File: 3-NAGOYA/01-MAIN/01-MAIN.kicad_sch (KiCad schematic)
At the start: 72 parts, among them J2 toLINE, J3 STS3032, J4 STS3032, J4 USB_C_Receptacle_USB2.0, J6 Front, J6 Top, Q1 2SA1015, SW1 NRST, SW2 BOOT0, U1 STM32F446RETx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

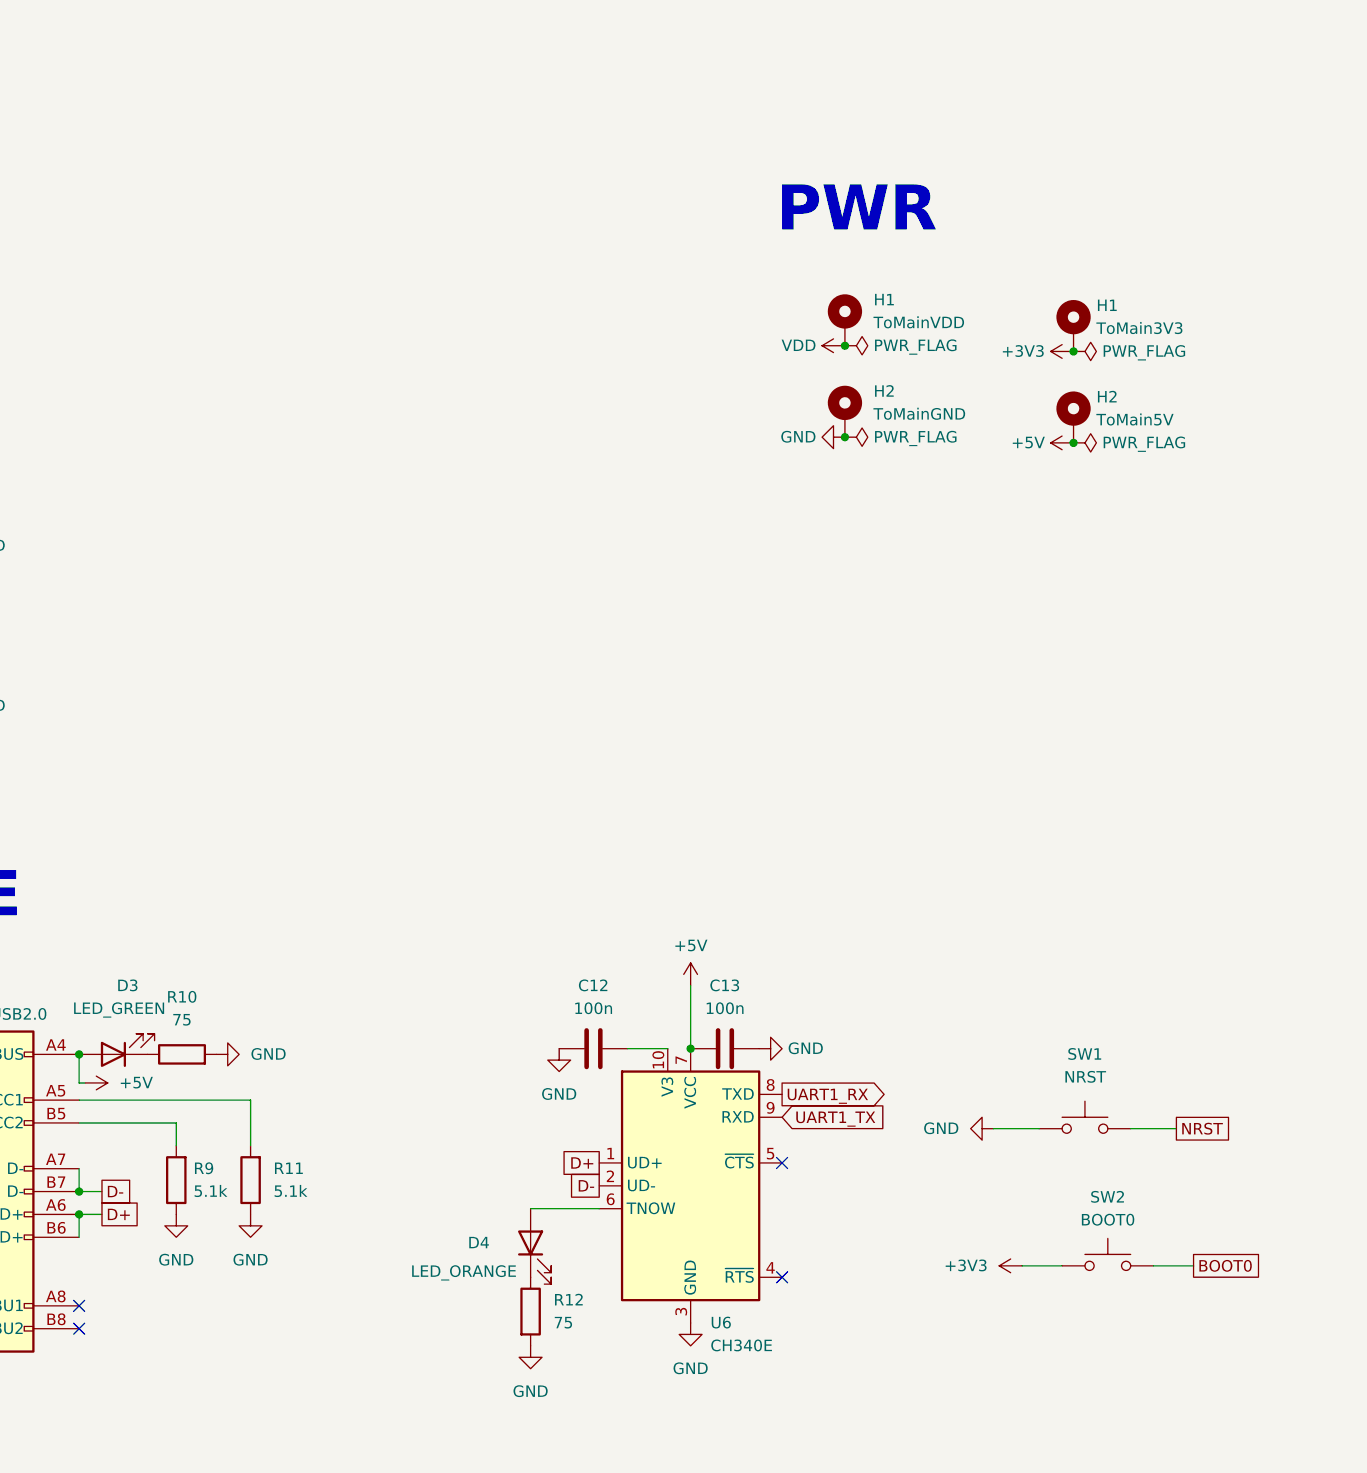
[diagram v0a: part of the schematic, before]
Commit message: 01-MAIN部品配置完了
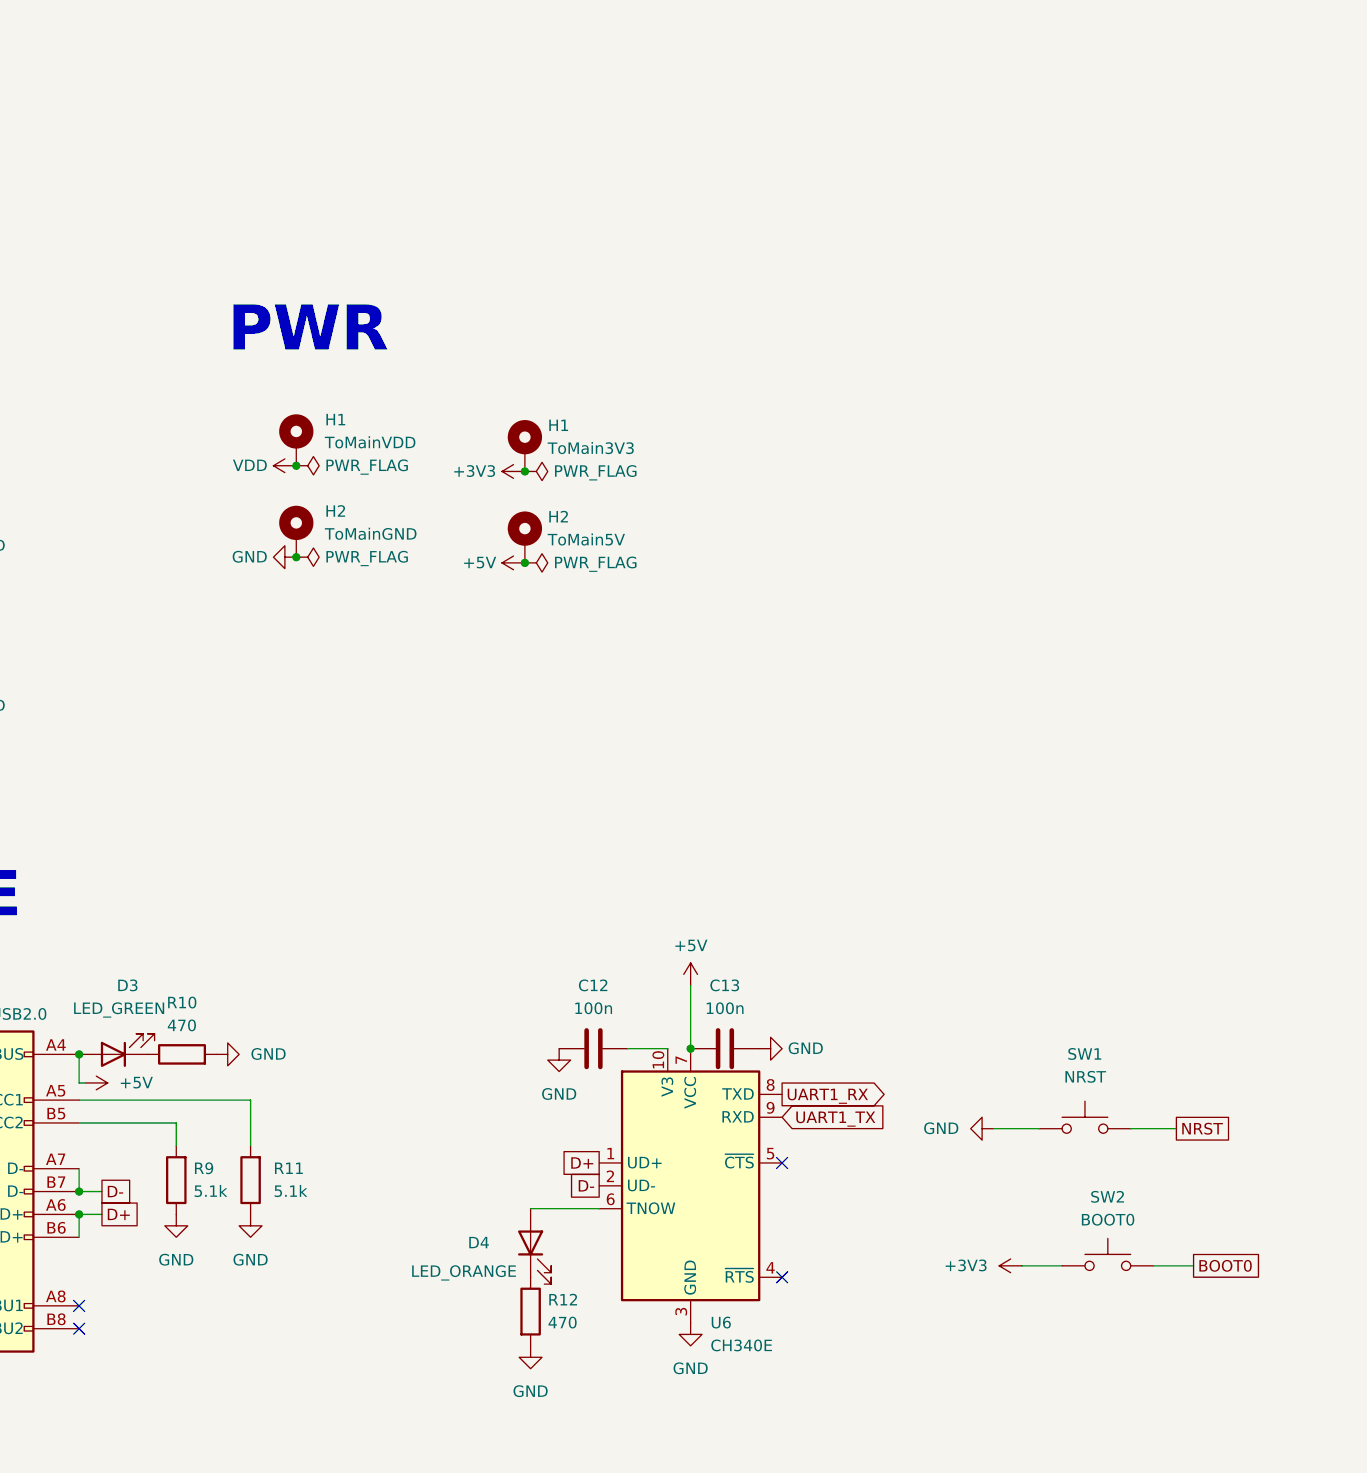
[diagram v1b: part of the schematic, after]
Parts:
- BZ1: footprint (none) -> Buzzer_Beeper:Buzzer_15x7.5RM7.6
- C12, C13: footprint Capacitor_SMD:C_0805_2012Metric -> Capacitor_SMD:C_0402_1005Metric; LCSC C49678 -> C1525
- D3: footprint LED_SMD:LED_1206_3216Metric -> LED_SMD:LED_0805_2012Metric; LCSC C499475 -> C2297
- D4: footprint LED_SMD:LED_1206_3216Metric -> LED_SMD:LED_0805_2012Metric; LCSC C2764895 -> C2296
- R10, R12: value 75 -> 470; footprint Resistor_SMD:R_0805_2012Metric -> Resistor_SMD:R_0603_1608Metric; LCSC C441974 -> C23179
- SW1, SW2: footprint Button_Switch_THT:SW_PUSH_6mm -> Akiduki:THBP07-043Cx
- U7, U8: LCSC (none) -> C9864
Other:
- moved on the sheet: H1, H2

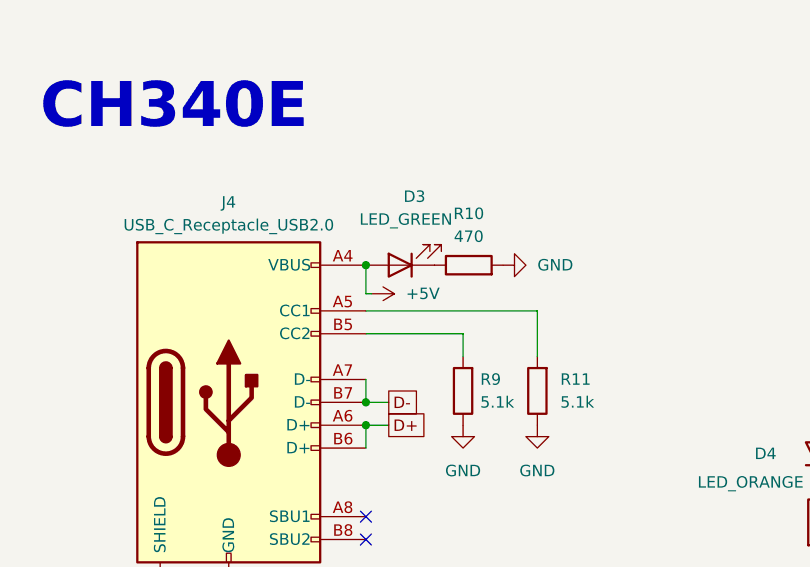
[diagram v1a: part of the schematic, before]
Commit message: 01-MAIN基板設計完了
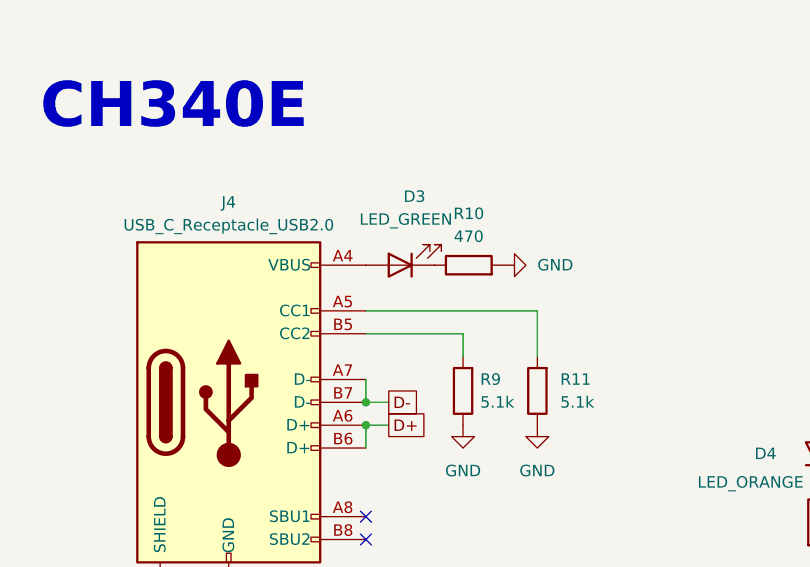
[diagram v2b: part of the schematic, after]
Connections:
- net +5V: no longer D3.2 (A), J4.A4 (VBUS), J4.A9 (VBUS), J4.B4 (VBUS), J4.B9 (VBUS)
- new net: D3.2 (A), J4.A4 (VBUS), J4.A9 (VBUS), J4.B4 (VBUS), J4.B9 (VBUS)
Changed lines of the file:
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@@
   (junction (at 229.235 234.95) (diameter 0) (color 0 0 0 0)
-  )
-  (junction (at 161.29 235.585) (diameter 0) (color 0 0 0 0)
   )
   (junction (at 210.82 170.815) (diameter 0) (color 0 0 0 0)
@@
     (stroke (width 0) (type default))
   )
-  (wire (pts (xy 161.925 238.76) (xy 161.29 238.76))
-    (stroke (width 0) (type default))
-  )
   (wire (pts (xy 318.77 61.595) (xy 318.77 62.865))
     (stroke (width 0) (type default))
@@
   )
   (wire (pts (xy 60.325 50.8) (xy 60.325 52.705))
-    (stroke (width 0) (type default))
-  )
-  (wire (pts (xy 161.29 238.76) (xy 161.29 235.585))
     (stroke (width 0) (type default))
   )
@@
         )
       )
-    )
-  )
-  (symbol (lib_id "power:+5V") (at 161.925 238.76 270) (unit 1)
-    (in_bom yes) (on_board yes) (dnp no) (fields_autoplaced)
-    (property "Reference" "#PWR035" (at 158.115 238.76 0)
-      (effects (font (size 1.27 1.27)) hide)
-    )
-    (property "Value" "+5V" (at 165.735 238.76 90)
-      (effects (font (size 1.27 1.27)) (justify left))
-    )
-    (property "Footprint" "" (at 161.925 238.76 0)
-      (effects (font (size 1.27 1.27)) hide)
-    )
-    (property "Datasheet" "" (at 161.925 238.76 0)
-      (effects (font (size 1.27 1.27)) hide)
-    )
-    (pin "1")
-    (instances
-      (project "01-MAIN"
-        (path "/8133ca0e-ad77-43a1-bab5-307f5494b57f"
-          (reference "#PWR035") (unit 1)
-        )
-      )
-      (project "06_WRITER"
-        (path "/816205b3-19fd-426f-b76d-aedd327993fe"
-          (reference "#PWR020") (unit 1)
-        )
-      )
